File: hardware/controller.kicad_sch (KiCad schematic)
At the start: 5 parts, among them Q1 BC848

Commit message: done routing
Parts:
- U5: value ~ -> Seeed-ESP32C3; footprint RF_WiFi:MCU_Seeed_ESP32C3_solder -> RF_Module:MCU_Seeed_ESP32C3_HandSolder
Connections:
- net +3V3: now also U5.19 (EN); no longer U5.23 (EN)
- net GND: now also U5.22 (GND); no longer U5.20 (GND)
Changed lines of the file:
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@@
 	(hierarchical_label "+3V3"
 		(shape input)
-		(at 147.32 85.09 0)
+		(at 147.32 86.36 0)
 		(fields_autoplaced yes)
 		(effects
@@
 	(hierarchical_label "+3V3"
 		(shape input)
-		(at 133.35 69.85 90)
+		(at 134.62 71.12 90)
 		(fields_autoplaced yes)
 		(effects
@@
 	(hierarchical_label "+5V"
 		(shape input)
-		(at 130.81 69.85 90)
+		(at 129.54 71.12 90)
 		(fields_autoplaced yes)
 		(effects
@@
 				(path "/ae153005-c1c4-4678-92de-98a47cf88e8d/421ee7c4-2a9c-4e65-b00b-3d6ff22b5783"
 					(reference "BZ1")
-					(unit 1)
-				)
-			)
-		)
-	)
-	(symbol
-		(lib_id "MCU_Seeed_ESP32C3:Seeed-ESP32C3")
-		(at 132.08 85.09 0)
-		(unit 1)
-		(exclude_from_sim no)
-		(in_bom yes)
-		(on_board yes)
-		(dnp no)
-		(fields_autoplaced yes)
-		(property "Reference" "U5"
-			(at 135.5441 66.04 0)
-			(effects
-				(font
-					(size 1.27 1.27)
-				)
-				(justify left)
-			)
-		)
-		(property "Value" "~"
-			(at 135.5441 68.58 0)
-			(effects
-				(font
-					(size 1.27 1.27)
-				)
-				(justify left)
-			)
-		)
-		(property "Footprint" "RF_WiFi:MCU_Seeed_ESP32C3_solder"
-			(at 135.5441 69.85 0)
-			(effects
-				(font
-					(size 1.27 1.27)
-				)
-				(justify left)
-			)
-		)
-		(property "Datasheet" ""
-			(at 132.08 85.09 0)
-			(effects
-				(font
-					(size 1.27 1.27)
-				)
-				(hide yes)
-			)
-		)
-		(property "Description" ""
-			(at 132.08 85.09 0)
-			(effects
-				(font
-					(size 1.27 1.27)
-				)
-				(hide yes)
-			)
-		)
-		(pin "6"
-		)
-		(pin "11"
-		)
-		(pin "14"
-		)
-		(pin "21"
-		)
-		(pin "13"
-		)
-		(pin "10"
-		)
-		(pin "12"
-		)
-		(pin "1"
-		)
-		(pin "20"
-		)
-		(pin "22"
-		)
-		(pin "24"
-		)
-		(pin "5"
-		)
-		(pin "23"
-		)
-		(pin "9"
-		)
-		(pin "19"
-		)
-		(pin "4"
-		)
-		(pin "8"
-		)
-		(pin "7"
-		)
-		(pin "2"
-		)
-		(pin "17"
-		)
-		(pin "15"
-		)
-		(pin "16"
-		)
-		(pin "3"
-		)
-		(instances
-			(project "Steuerplatine"
-				(path "/ae153005-c1c4-4678-92de-98a47cf88e8d/421ee7c4-2a9c-4e65-b00b-3d6ff22b5783"
-					(reference "U5")
 					(unit 1)
 				)
@@
 					(unit 1)
 				)
+			)
+		)
+	)
+	(symbol
+		(lib_name "Seeed-ESP32C3_1")
+		(lib_id "MCU_Seeed_ESP32C3:Seeed-ESP32C3")
+		(at 132.08 88.9 0)
+		(unit 1)
+		(exclude_from_sim no)
+		(in_bom yes)
+		(on_board yes)
+		(dnp no)
+		(fields_autoplaced yes)
+		(property "Reference" "U5"
+			(at 136.8141 68.58 0)
+			(effects
+				(font
+					(size 1.27 1.27)
+				)
+				(justify left)
+			)
+		)
+		(property "Value" "Seeed-ESP32C3"
+			(at 136.8141 71.12 0)
+			(effects
+				(font
+					(size 1.27 1.27)
+				)
+				(justify left)
+			)
+		)
+		(property "Footprint" "RF_Module:MCU_Seeed_ESP32C3_HandSolder"
+			(at 132.842 117.094 0)
+			(effects
+				(font
+					(size 1.27 1.27)
+				)
+				(hide yes)
+			)
+		)
+		(property "Datasheet" "https://wiki.seeedstudio.com/XIAO_ESP32C3_Getting_Started/"
+			(at 132.588 119.126 0)
+			(effects
+				(font
+					(size 1.27 1.27)
+				)
+				(hide yes)
+			)
+		)
+		(property "Description" "Wifi Module based on ESP32C3"
+			(at 132.08 85.09 0)
+			(effects
+				(font
+					(size 1.27 1.27)
+				)
+				(hide yes)
+			)
+		)
+		(pin "8"
+		)
+		(pin "14"
+		)
+		(pin "18"
+		)
+		(pin "17"
+		)
+		(pin "3"
+		)
+		(pin "10"
+		)
+		(pin "13"
+		)
+		(pin "12"
+		)
+		(pin "11"
+		)
+		(pin "1"
+		)
+		(pin "6"
+		)
+		(pin "7"
+		)
+		(pin "4"
+		)
+		(pin "21"
+		)
+		(pin "20"
+		)
+		(pin "19"
+		)
+		(pin "2"
+		)
+		(pin "23"
+		)
+		(pin "16"
+		)
+		(pin "5"
+		)
+		(pin "9"
+		)
+		(pin "22"
+		)
+		(pin "15"
+		)
+		(instances
+			(project "Steuerplatine"
+				(path "/ae153005-c1c4-4678-92de-98a47cf88e8d/421ee7c4-2a9c-4e65-b00b-3d6ff22b5783"
+					(reference "U5")
+					(unit 1)
+				)

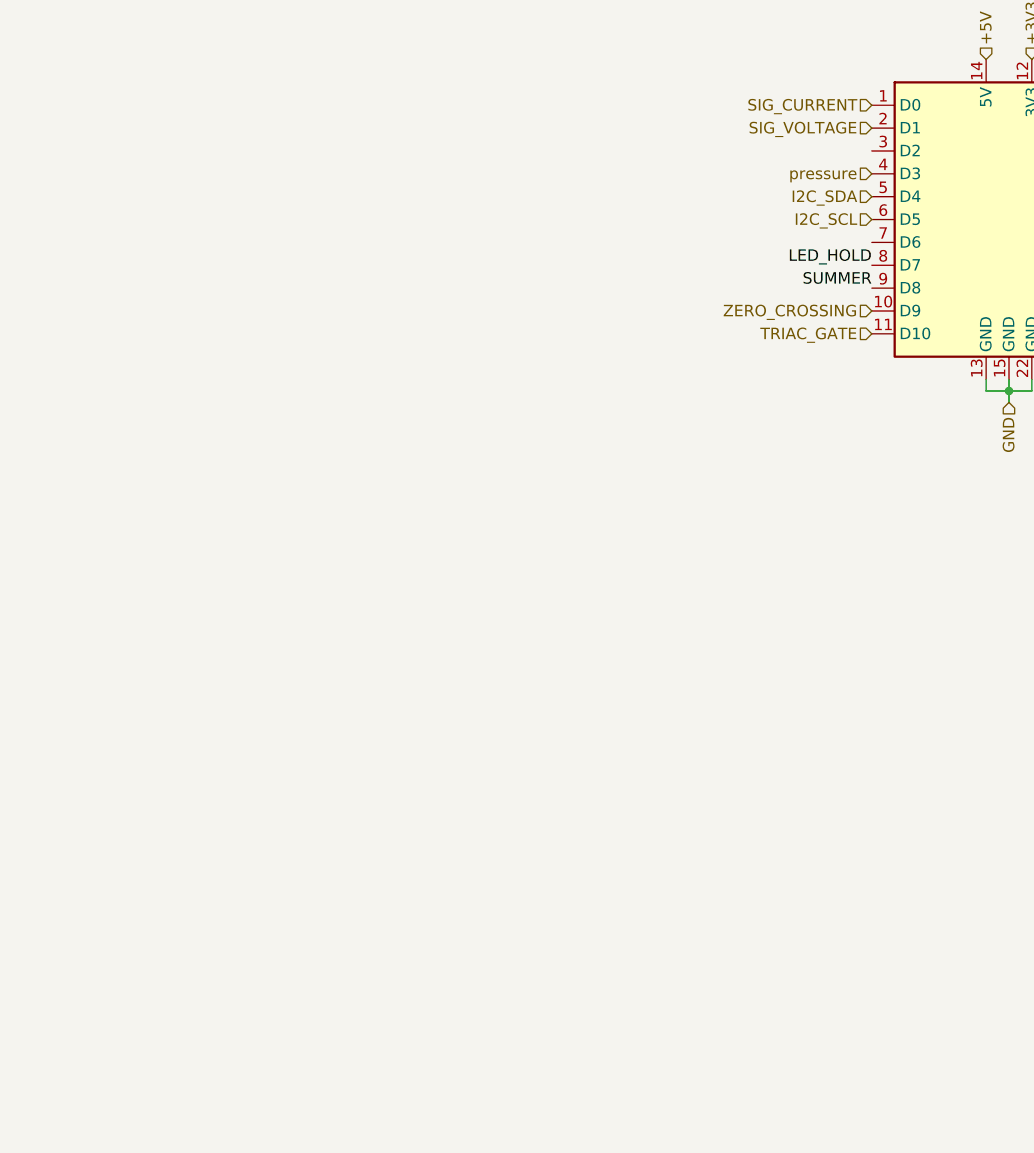
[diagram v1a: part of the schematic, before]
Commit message: added pressure sensor
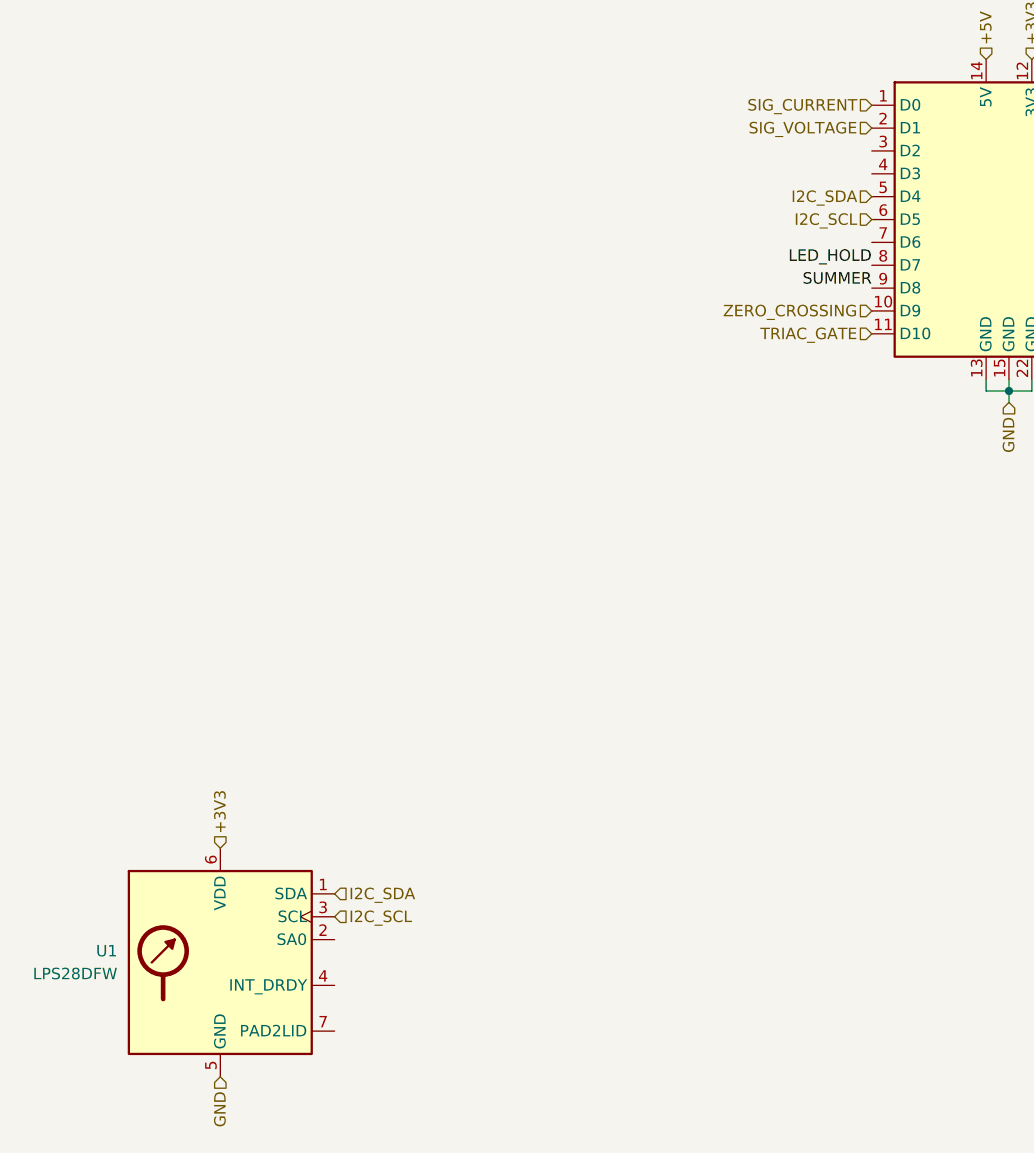
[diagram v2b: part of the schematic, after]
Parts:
- added U1: LPS28DFW, Sensor_Pressure:ST_LPS28DFW, symbol Sensor_Pressure:LPS28DFW
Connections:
- net +3V3: now also U1.6 (VDD)
- net GND: now also U1.5 (GND)
- net I2C_SCL: now also U1.3 (SCL)
- net I2C_SDA: now also U1.1 (SDA)
- net pressure: no longer names the net of U5.4 (D3)
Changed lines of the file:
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@@
 	(hierarchical_label "+3V3"
 		(shape input)
+		(at 44.45 158.75 90)
+		(fields_autoplaced yes)
+		(effects
+			(font
+				(size 1.27 1.27)
+			)
+			(justify left)
+		)
+	)
+	(hierarchical_label "+3V3"
+		(shape input)
 		(at 147.32 86.36 0)
 		(fields_autoplaced yes)
@@
 		)
 	)
-	(hierarchical_label "pressure"
-		(shape input)
-		(at 116.84 83.82 180)
-		(fields_autoplaced yes)
-		(effects
-			(font
-				(size 1.27 1.27)
-			)
-			(justify right)
-		)
-	)
 	(hierarchical_label "GND"
 		(shape input)
+		(at 44.45 184.15 270)
+		(fields_autoplaced yes)
+		(effects
+			(font
+				(size 1.27 1.27)
+			)
+			(justify right)
+		)
+	)
+	(hierarchical_label "GND"
+		(shape input)
 		(at 132.08 109.22 270)
 		(fields_autoplaced yes)
@@
 		)
 	)
+	(hierarchical_label "I2C_SDA"
+		(shape input)
+		(at 57.15 163.83 0)
+		(fields_autoplaced yes)
+		(effects
+			(font
+				(size 1.27 1.27)
+			)
+			(justify left)
+		)
+	)
 	(hierarchical_label "+5V"
 		(shape input)
@@
 			)
 			(justify right)
+		)
+	)
+	(hierarchical_label "I2C_SCL"
+		(shape input)
+		(at 57.15 166.37 0)
+		(fields_autoplaced yes)
+		(effects
+			(font
+				(size 1.27 1.27)
+			)
+			(justify left)
 		)
 	)
@@
 					(unit 1)
 				)
+			)
+		)
+	)
+	(symbol
+		(lib_id "Sensor_Pressure:LPS28DFW")
+		(at 44.45 171.45 0)
+		(unit 1)
+		(exclude_from_sim no)
+		(in_bom yes)
+		(on_board yes)
+		(dnp no)
+		(fields_autoplaced yes)
+		(property "Reference" "U1"
+			(at 33.02 170.1799 0)
+			(effects
+				(font
+					(size 1.27 1.27)
+				)
+				(justify right)
+			)
+		)
+		(property "Value" "LPS28DFW"
+			(at 33.02 172.7199 0)
+			(effects
+				(font
+					(size 1.27 1.27)
+				)
+				(justify right)
+			)
+		)
+		(property "Footprint" "Sensor_Pressure:ST_LPS28DFW"
+			(at 45.72 182.88 0)
+			(effects
+				(font
+					(size 1.27 1.27)
+				)
+				(justify left)
+				(hide yes)
+			)
+		)
+		(property "Datasheet" "https://www.st.com/resource/en/datasheet/lps28dfw.pdf"
+			(at 45.72 185.42 0)
+			(effects
+				(font
+					(size 1.27 1.27)
+				)
+				(justify left)
+				(hide yes)
+			)
+		)
+		(property "Description" "MEMS nano pressure sensor, 260-4060 hPa, absolute digital output baromeeter, 24 bit, I2C, 0.32 Pa noise rms"
+			(at 44.45 196.85 0)
+			(effects
+				(font
+					(size 1.27 1.27)
+				)
+				(hide yes)
+			)
+		)
+		(pin "4"
+		)
+		(pin "3"
+		)
+		(pin "2"
+		)
+		(pin "1"
+		)
+		(pin "5"
+		)
+		(pin "6"
+		)
+		(pin "7"
+		)
+		(instances
+			(project "Steuerplatine"
+				(path "/ae153005-c1c4-4678-92de-98a47cf88e8d/421ee7c4-2a9c-4e65-b00b-3d6ff22b5783"
+					(reference "U1")
+					(unit 1)
+				)

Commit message: added some zones
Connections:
- net GND: now also U1.7 (PAD2LID)
- net pressure_interrupt: now reaches U1.4 (INT_DRDY)
- net pressure_interrupt: now also U5.7 (D6)
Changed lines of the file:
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@@
+		)
+	)
+	(label "pressure_interrupt"
+		(at 57.15 173.99 0)
+		(fields_autoplaced yes)
+		(effects
+			(font
+				(size 1.27 1.27)
+			)
+			(justify left bottom)
 		)
 	)
@@
 		)
 	)
+	(label "pressure_interrupt"
+		(at 116.84 91.44 180)
+		(fields_autoplaced yes)
+		(effects
+			(font
+				(size 1.27 1.27)
+			)
+			(justify right bottom)
+		)
+	)
+	(hierarchical_label "GND"
+		(shape input)
+		(at 57.15 179.07 0)
+		(fields_autoplaced yes)
+		(effects
+			(font
+				(size 1.27 1.27)
+			)
+			(justify left)
+		)
+	)

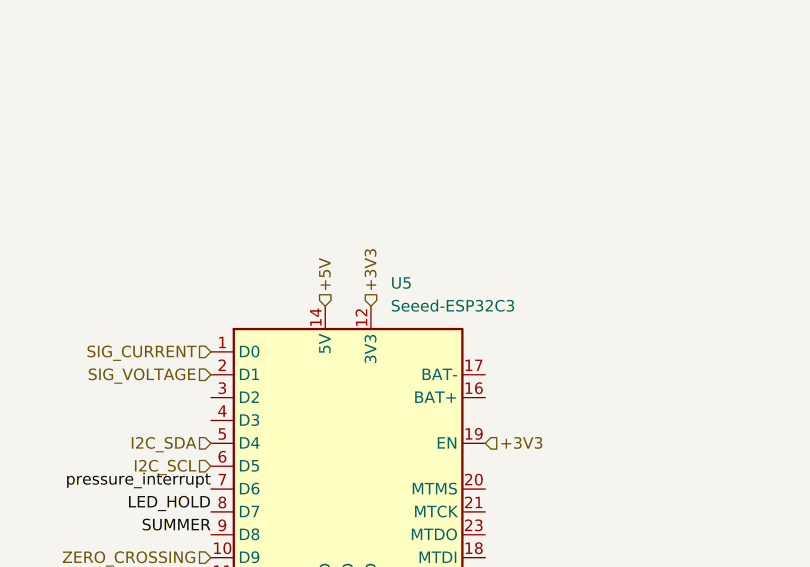
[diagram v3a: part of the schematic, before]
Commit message: added some datasheets
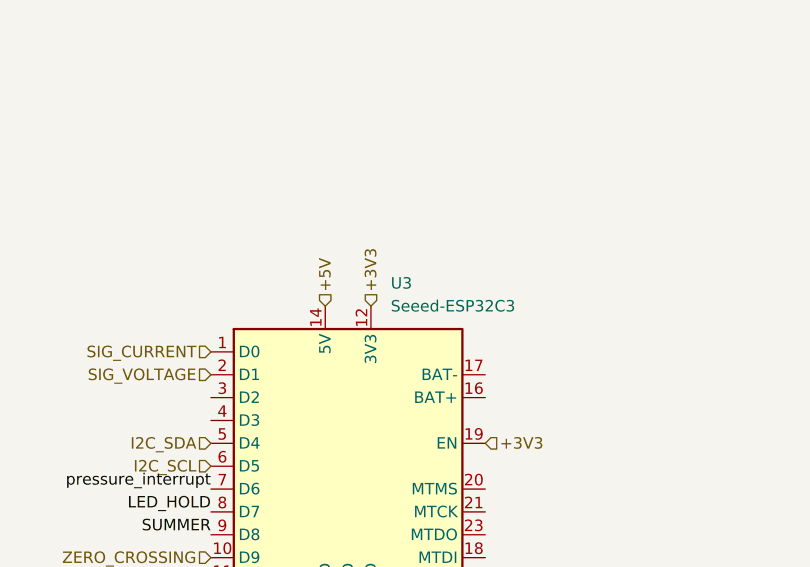
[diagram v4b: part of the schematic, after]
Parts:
- removed U5: Seeed-ESP32C3, RF_Module:MCU_Seeed_ESP32C3_HandSolder, symbol MCU_Seeed_ESP32C3:Seeed-ESP32C3
- added U3: Seeed-ESP32C3, RF_Module:MCU_Seeed_ESP32C3, symbol MCU_Seeed_ESP32C3:Seeed-ESP32C3
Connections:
- net +3V3: now also U3.12 (3V3), U3.19 (EN)
- net +5V: now also U3.14 (5V)
- net GND: now also U3.13 (GND), U3.15 (GND), U3.22 (GND)
- net I2C_SCL: now also U3.6 (D5)
- net I2C_SDA: now also U3.5 (D4)
- net LED_HOLD: now also U3.8 (D7)
- net SIG_CURRENT: now also U3.1 (D0)
- net SIG_VOLTAGE: now also U3.2 (D1)
- net SUMMER: now also U3.9 (D8)
- net TRIAC_GATE: now also U3.11 (D10)
- net ZERO_CROSSING: now also U3.10 (D9)
- net pressure_interrupt: now also U3.7 (D6)
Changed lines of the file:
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@@
 	)
 	(symbol
-		(lib_name "Seeed-ESP32C3_1")
 		(lib_id "MCU_Seeed_ESP32C3:Seeed-ESP32C3")
 		(at 132.08 88.9 0)
@@
 		(dnp no)
 		(fields_autoplaced yes)
-		(property "Reference" "U5"
+		(property "Reference" "U3"
 			(at 136.8141 68.58 0)
 			(effects
@@
 			)
 		)
-		(property "Footprint" "RF_Module:MCU_Seeed_ESP32C3_HandSolder"
+		(property "Footprint" "RF_Module:MCU_Seeed_ESP32C3"
 			(at 132.842 117.094 0)
 			(effects
@@
 			)
 		)
-		(pin "8"
+		(pin "19"
+		)
+		(pin "4"
+		)
+		(pin "20"
+		)
+		(pin "17"
+		)
+		(pin "22"
+		)
+		(pin "3"
+		)
+		(pin "2"
+		)
+		(pin "18"
+		)
+		(pin "23"
+		)
+		(pin "6"
+		)
+		(pin "21"
 		)
 		(pin "14"
 		)
-		(pin "18"
-		)
-		(pin "17"
-		)
-		(pin "3"
-		)
-		(pin "10"
+		(pin "1"
 		)
 		(pin "13"
@@
 		(pin "11"
 		)
-		(pin "1"
-		)
-		(pin "6"
-		)
-		(pin "7"
-		)
-		(pin "4"
-		)
-		(pin "21"
-		)
-		(pin "20"
-		)
-		(pin "19"
-		)
-		(pin "2"
-		)
-		(pin "23"
+		(pin "10"
 		)
 		(pin "16"
@@
 		(pin "5"
 		)
+		(pin "7"
+		)
 		(pin "9"
 		)
-		(pin "22"
+		(pin "15"
 		)
-		(pin "15"
+		(pin "8"
 		)
 		(instances
 			(project "Steuerplatine"
 				(path "/ae153005-c1c4-4678-92de-98a47cf88e8d/421ee7c4-2a9c-4e65-b00b-3d6ff22b5783"
-					(reference "U5")
+					(reference "U3")
 					(unit 1)
 				)

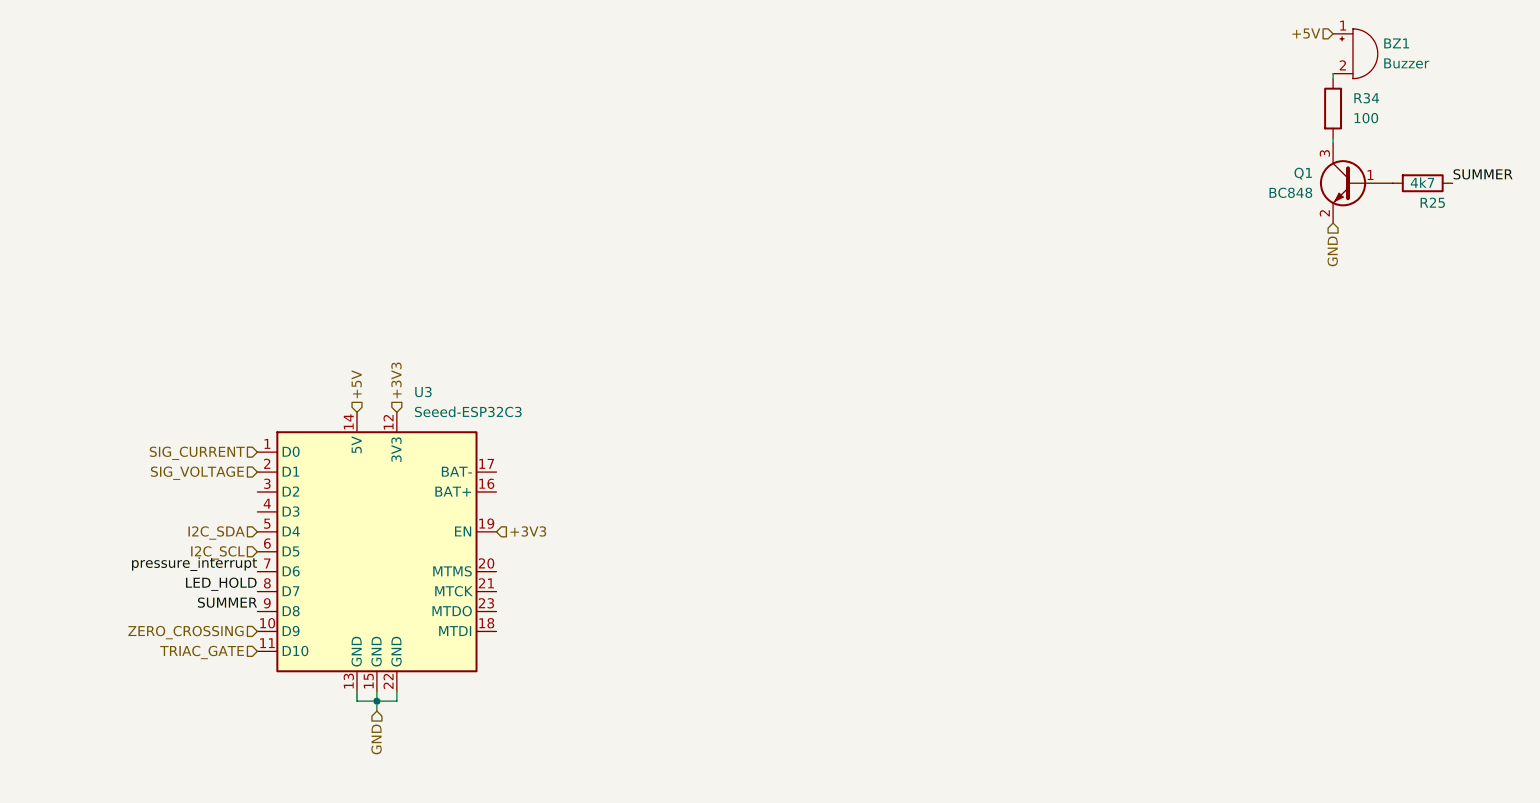
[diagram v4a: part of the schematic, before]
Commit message: some more rules and routings
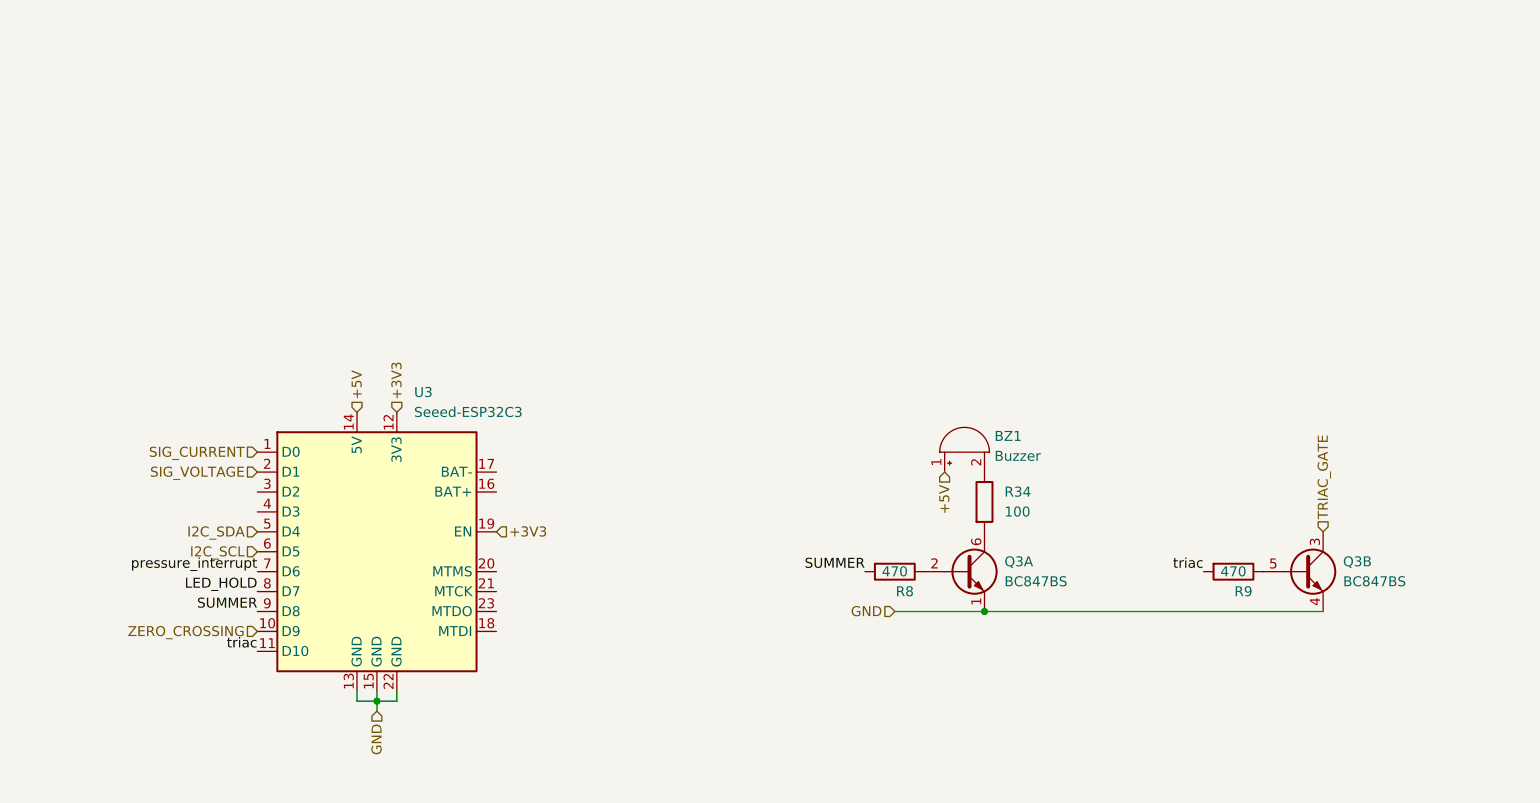
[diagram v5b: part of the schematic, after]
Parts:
- removed Q1: BC848, Package_TO_SOT_SMD:SOT-23, symbol Transistor_BJT:BC848
- removed R25: 4k7, Resistor_SMD:R_0603_1608Metric, symbol Device:R
- added Q3: BC847BS, Package_TO_SOT_SMD:SOT-363_SC-70-6, symbol Transistor_BJT:BC847BS
- added R8, R9: 470, Resistor_SMD:R_0603_1608Metric, symbol Device:R
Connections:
- net GND: now also Q3.1 (E1), Q3.4 (E2)
- net SUMMER: now also R8.2
- net TRIAC_GATE: now also Q3.3 (C2); no longer U3.11 (D10)
- net at R34.2: now also Q3.6 (C1)
- new net: Q3.5 (B2), R9.1
- new net: Q3.2 (B1), R8.1
- new net triac: R9.2, U3.11 (D10)
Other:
- moved on the sheet: BZ1, R34
